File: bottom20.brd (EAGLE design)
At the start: 160 x 140 mm, 145 parts, among them J1 TX, J2 RX, T1:IC1 MULTIPLEXER, T1:R1 20k, T1:R10 20k, T1:R11 20k, T1:R12 20k, T1:R13 20k, T1:R14 20k, T1:R15 20k, T1:R16 20k, T1:R17 10k, T1:R2 20k, T1:R3 20k, T1:R4 20k, T1:R5 20k, T1:R6 20k, T1:R7 20k, T1:R8 20k, T1:R9 20k, T1:T1 SFH320, T1:T10 SFH320, T1:T11 SFH320, T1:T12 SFH320, T1:T13 SFH320, T1:T14 SFH320, T1:T15 SFH320, T1:T16 SFH320, T1:T2 SFH320, T1:T3 SFH320, T1:T4 SFH320, T1:T5 SFH320, T1:T6 SFH320, T1:T7 SFH320, T1:T8 SFH320, T1:T9 SFH320, T2:IC1 MULTIPLEXER, T2:R1 20k, T2:R10 20k, T2:R11 20k, T2:R12 20k, T2:R13 20k, T2:R14 20k, T2:R15 20k, T2:R16 20k, T2:R17 10k, T2:R2 20k, T2:R3 20k, T2:R4 20k, T2:R5 20k, T2:R6 20k, T2:R7 20k, T2:R8 20k, T2:R9 20k, T2:T1 SFH320, T2:T10 SFH320, T2:T11 SFH320, T2:T12 SFH320, T2:T13 SFH320, T2:T14 SFH320, T2:T15 SFH320, T2:T16 SFH320, T2:T2 SFH320, T2:T3 SFH320, T2:T4 SFH320, T2:T5 SFH320, T2:T6 SFH320, T2:T7 SFH320, T2:T8 SFH320, T2:T9 SFH320

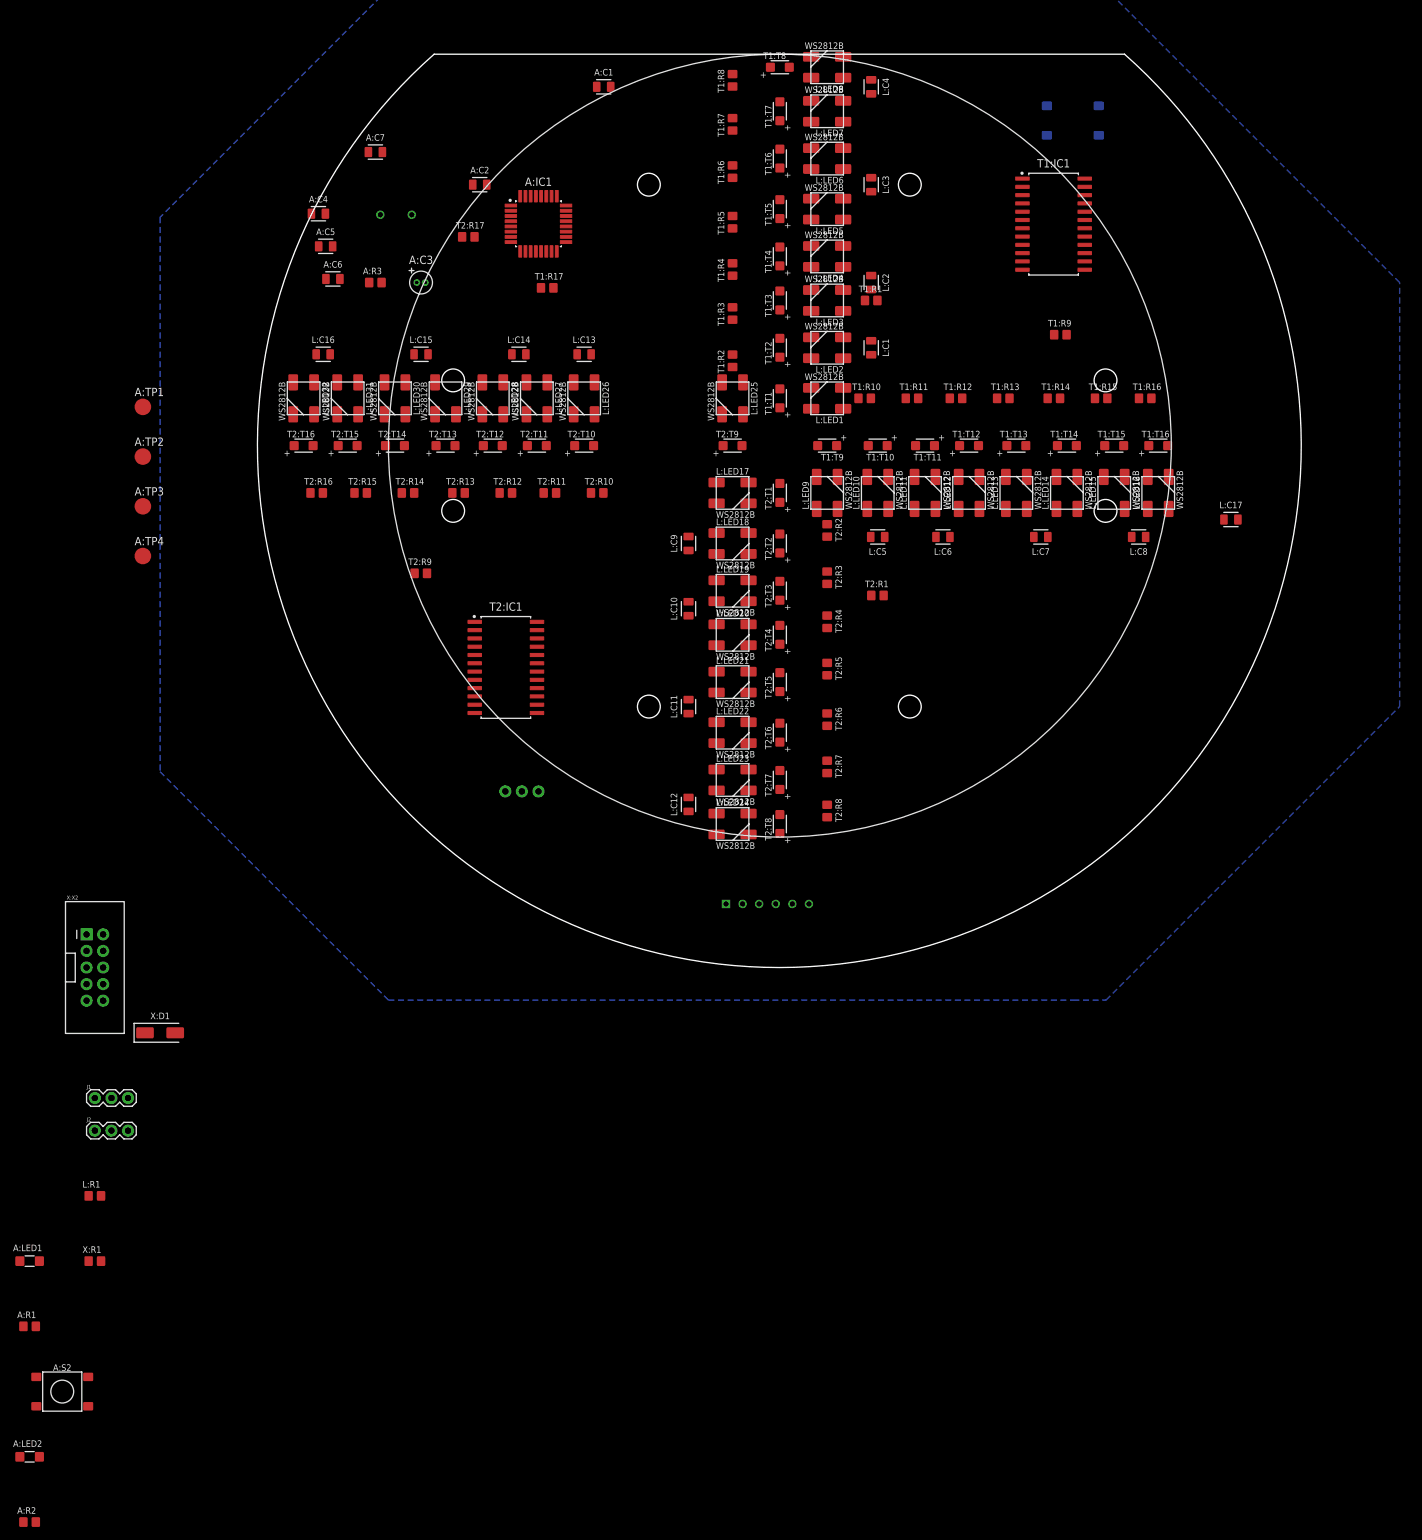
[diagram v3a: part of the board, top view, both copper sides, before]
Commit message: - bot.brd (layout changes)
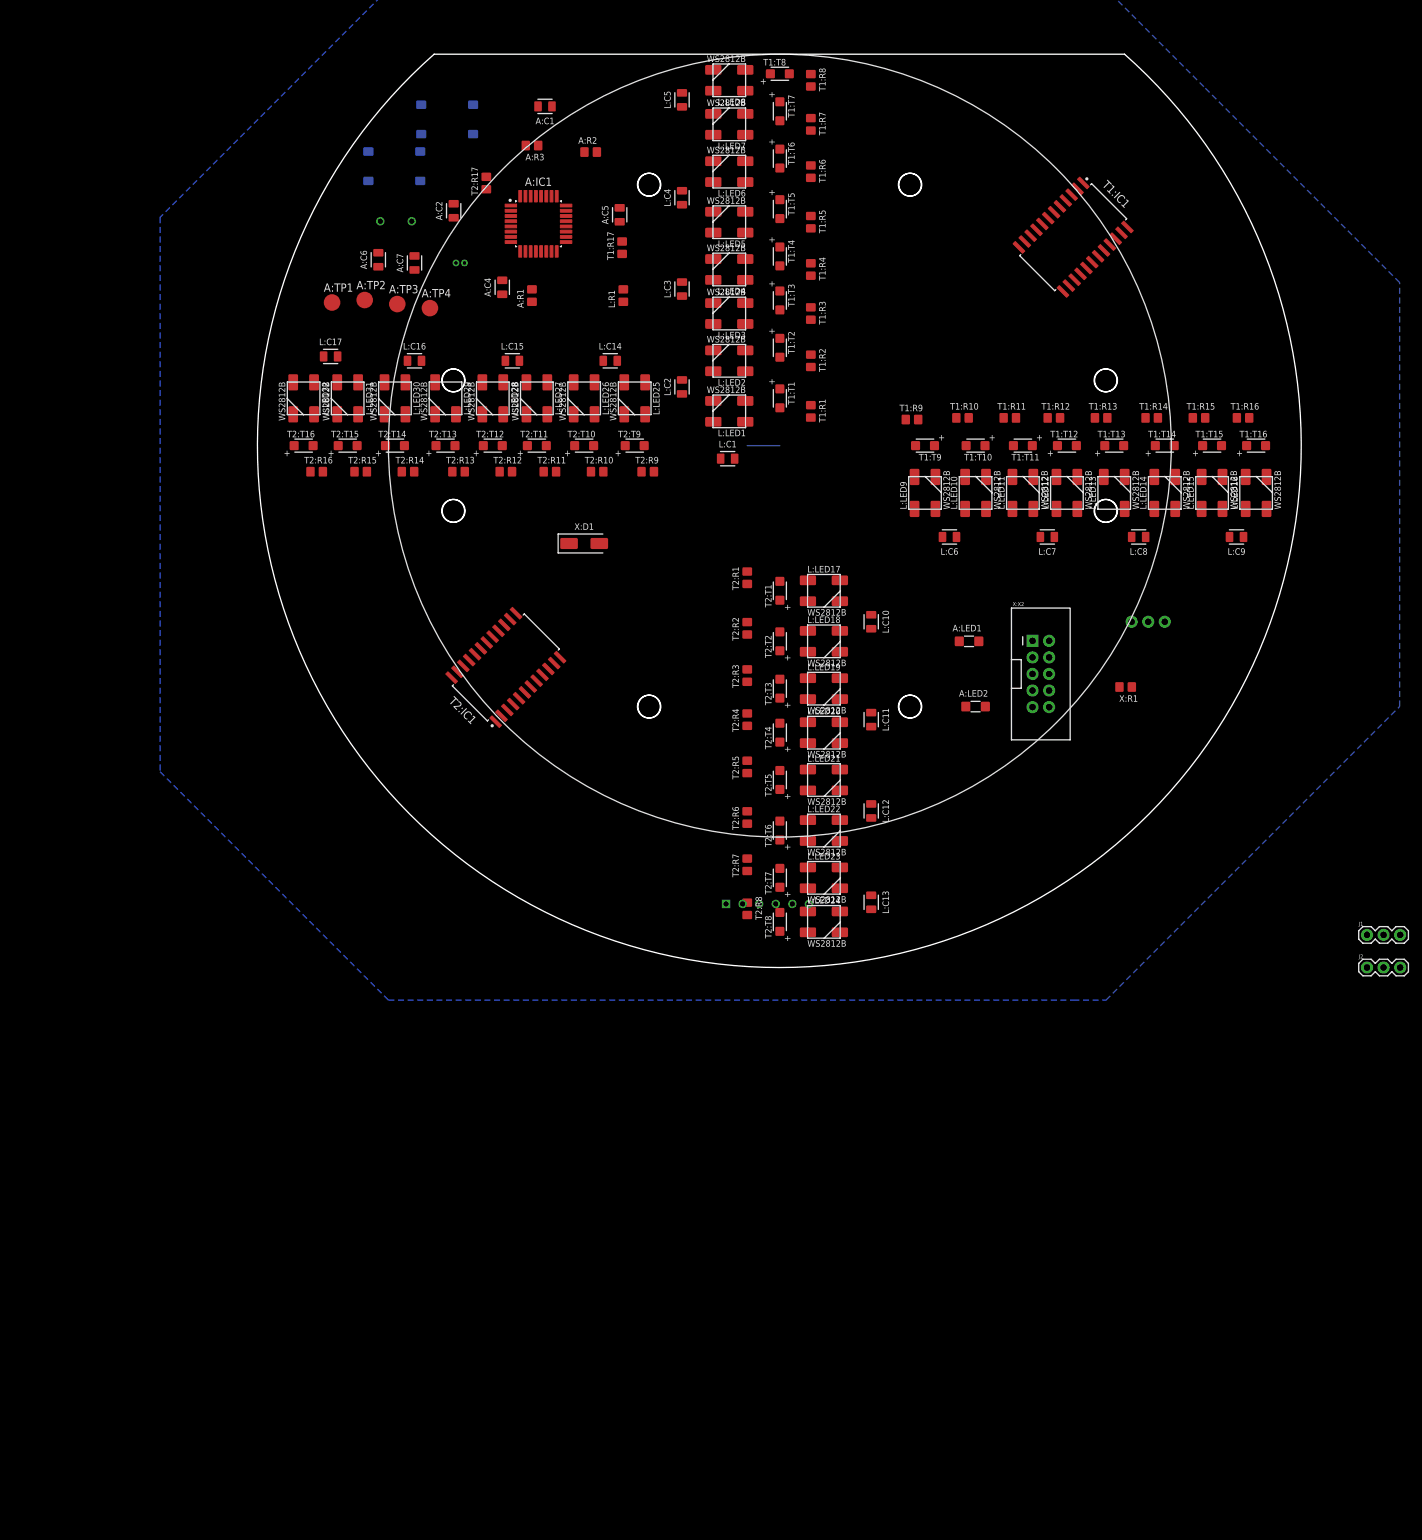
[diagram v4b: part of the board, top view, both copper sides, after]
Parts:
- moved A:R2 226.9 mm to (-29.0, 45.0)
- moved A:S2 203.7 mm to (-51.0, 50.0), flipped to the bottom
- moved J1 196.6 mm to (90.0, -75.0)
- moved J2 196.6 mm to (90.0, -80.0)
- moved A:LED2 185.1 mm to (30.0, -40.0)
- moved X:R1 180.9 mm to (53.0, -37.0), turned to 180 degrees
- moved A:R1 175.8 mm to (-38.0, 23.0), turned to 90 degrees
- moved A:LED1 172.5 mm to (29.0, -30.0)
- moved L:R1 160.0 mm to (-24.0, 23.0), turned to 90 degrees
- moved X:X2 151.8 mm to (40.0, -35.0)
- moved L:C17 140.2 mm to (-68.9, 13.7)
- moved A:S1 104.2 mm to (-59.1, 42.8)
- moved P:X3 99.5 mm to (59.0, -27.0)
- moved X:D1 99.2 mm to (-30.0, -15.0)
- moved L:C13 94.8 mm to (14.0, -70.0), turned to 270 degrees
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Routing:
- net N$19: track 0.00 -> 5.00 mm

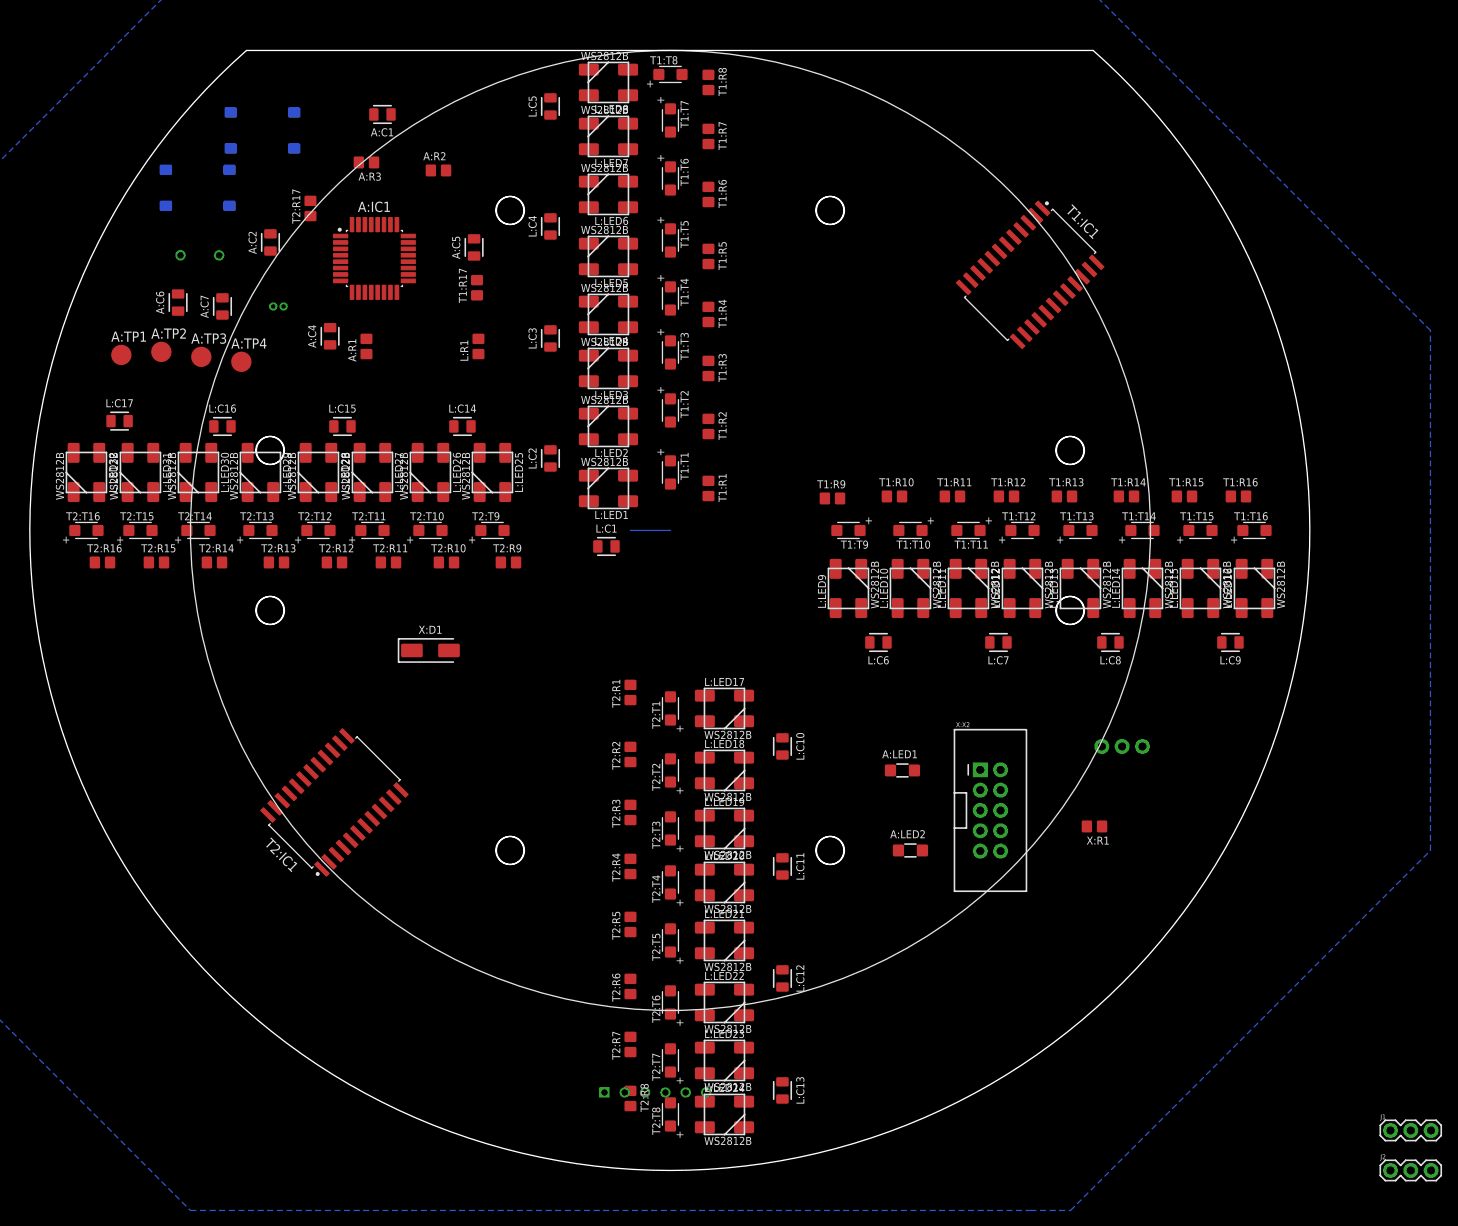
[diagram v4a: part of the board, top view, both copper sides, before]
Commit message: - bot.sch (layout perfections)
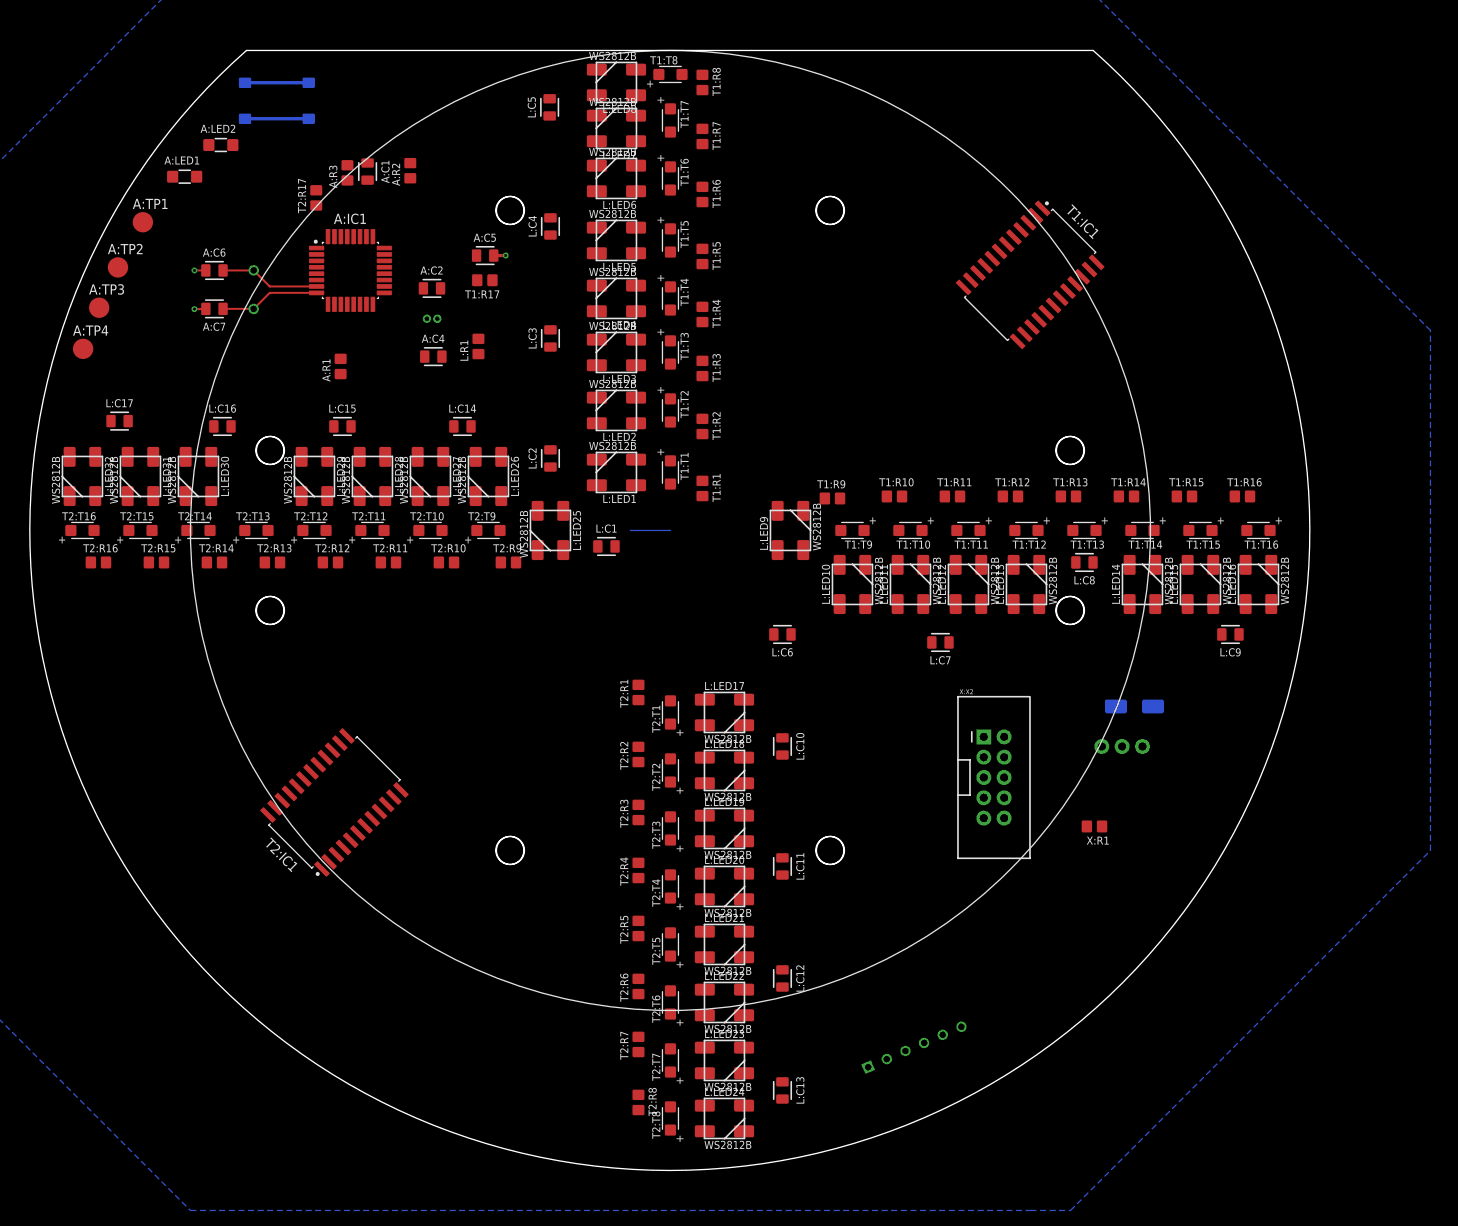
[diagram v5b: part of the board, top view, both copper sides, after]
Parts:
- removed A:S1: SMD-BUTTON, iceberg20:SWITCH-6MM-SMD
- removed J1: TX, iceberg20:3X1
- removed J2: RX, iceberg20:3X1
- moved A:LED2 123.3 mm to (-56.2, 48.2)
- moved A:LED1 116.4 mm to (-60.7, 44.2)
- moved X:D1 88.3 mm to (58.0, -22.0), flipped to the bottom
- moved X:X1 33.1 mm to (23.0, -67.5), turned to 156.6 degrees
- moved A:C2 21.0 mm to (-29.8, 30.3), turned to 0 degrees
- moved A:TP4 19.8 mm to (-73.4, 22.7)
- moved A:C3 19.3 mm to (-29.8, 26.5), turned to 180 degrees
- moved A:TP1 16.8 mm to (-66.0, 38.5)
- moved A:TP3 14.2 mm to (-71.4, 27.8)
- moved A:C4 13.2 mm to (-29.6, 21.7), turned to 0 degrees
- moved L:C6 12.0 mm to (14.0, -13.0)
- moved A:TP2 11.9 mm to (-69.1, 32.9)
- moved L:C8 10.5 mm to (51.8, -4.00)
- moved L:LED25 10.3 mm to (-15.0, 0.00)
- moved L:LED9 10.3 mm to (15.0, 0.00)
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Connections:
- removed net ARD-RX: J2.3
- removed net ARD-TX: J1.3
- removed net N$14: A:IC1.31, J1.2
- removed net N$15: A:IC1.30, J2.2
- net ARD-RESET: no longer A:S1.A1, A:S1.A2
- net GND: no longer A:S1.B1, A:S1.B2
- net RX: now also A:IC1.30; no longer J2.1
- net TX: now also A:IC1.31; no longer J1.1
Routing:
- net A:N$3: track 0.00 -> 12.5 mm
- net A:N$2: track 0.00 -> 12.5 mm
- net GND: track 0.00 -> 12.3 mm, vias 0 -> 3
- net A:N$9: track 0.00 -> 7.95 mm

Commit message: - bot.brd/sch (begin of routing)
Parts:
- moved L:R1 72.5 mm to (30.1, -25.3), turned to 0 degrees
- moved A:TP1 36.3 mm to (-34.6, 20.3)
- moved A:TP2 32.5 mm to (-39.2, 20.3)
- moved X:R1 30.8 mm to (27.1, -20.3)
- moved A:R1 28.1 mm to (-55.0, 45.0), turned to 180 degrees
- moved A:TP3 28.0 mm to (-44.5, 20.1)
- moved A:TP4 23.2 mm to (-50.4, 20.2)
- moved X:D1 20.0 mm to (52.8, -41.3), turned to 180 degrees
- moved A:LED2 9.98 mm to (-50.0, 56.0), turned to 180 degrees
- moved P:X3 8.36 mm to (52.1, -31.7), turned to 315 degrees
- moved A:C4 5.79 mm to (-30.0, 27.5)
- moved A:S2 5.48 mm to (-53.2, 50.0)
- moved A:R2 4.28 mm to (-36.8, 45.0)
- moved T2:R17 3.64 mm to (-46.9, 39.0), turned to 0 degrees
- moved T1:R9 3.00 mm to (23.2, 4.00), turned to 180 degrees
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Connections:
- net N$1 renamed X:+12V
- removed net X:LED-IN: X:X2.6
- new net X:+5V: X:D1.1
- net +5V: no longer X:D1.1
- net LED-IN: now also X:X2.6
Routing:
- net GND: track 12.3 -> 221.6 mm, vias 3 -> 10
- net T1:N$9: track 0.00 -> 53.1 mm
- net T1:N$10: track 0.00 -> 50.0 mm
- net T1:N$2: track 0.00 -> 48.8 mm
- net T1:N$3: track 0.00 -> 47.7 mm
- net T1:N$5: track 0.00 -> 47.5 mm
- net T1:N$11: track 0.00 -> 46.9 mm
- net T1:N$4: track 0.00 -> 46.0 mm
- net T1:N$25: track 0.00 -> 42.0 mm
- net T1:N$7: track 0.00 -> 41.0 mm
- net T1:N$22: track 0.00 -> 37.9 mm
- net T1:N$12: track 0.00 -> 37.5 mm
- net T1:N$14: track 0.00 -> 35.4 mm
- net T1:N$20: track 0.00 -> 34.4 mm
- net T1:N$18: track 0.00 -> 34.3 mm
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- added copper zone on layer 1, net +5V

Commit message: - bot.brd (Routing)
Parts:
- moved A:C2 112.1 mm to (54.4, -43.4)
- moved A:C3 112.1 mm to (54.8, -50.4)
- moved A:C4 112.1 mm to (54.4, -46.4)
- moved A:C5 112.1 mm to (61.4, -39.9)
- moved A:C6 112.1 mm to (27.4, -41.4)
- moved A:C7 112.1 mm to (27.4, -46.2)
- moved A:IC1 112.1 mm to (44.4, -41.4)
- moved A:LED1 112.1 mm to (23.6, -28.9)
- moved A:LED2 112.1 mm to (34.4, -17.9)
- moved A:Q1 112.1 mm to (32.3, -43.8)
- moved A:R1 112.1 mm to (29.4, -28.9)
- moved A:R2 112.1 mm to (47.6, -28.9)
- moved A:S2 112.1 mm to (31.1, -23.9)
- moved A:TP1 112.1 mm to (49.8, -53.6)
- moved A:TP2 112.1 mm to (45.2, -53.6)
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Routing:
- net +5V: track 12.1 -> 250.3 mm, vias 0 -> 17
- net GND: track 221.6 -> 302.5 mm, vias 10 -> 9
- net L:CON-1: track 0.00 -> 73.4 mm
- net T1:N$1: track 4.00 -> 50.5 mm, vias 0 -> 2
- net X:N$1: track 16.5 -> 0.00 mm
- net LED-IN: track 10.4 -> 0.00 mm
- net L:N$9: track 0.00 -> 5.32 mm
- net T2:N$7: track 0.00 -> 4.00 mm
- net T2:N$5: track 0.00 -> 4.00 mm
- net T2:N$4: track 0.00 -> 4.00 mm
- net T2:N$3: track 0.00 -> 4.00 mm
- net T2:N$26: track 0.00 -> 4.00 mm
- net T2:N$25: track 0.00 -> 4.00 mm
- net T2:N$22: track 0.00 -> 4.00 mm
- net T2:N$20: track 0.00 -> 4.00 mm
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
